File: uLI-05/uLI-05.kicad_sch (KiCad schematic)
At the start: 51 parts, among them J1 STL1550, J2 USB_B, J3 RJ25, J4 RJ25, J5 PROG, Q1 IRF7306, U1 LM78M05_TO252, U2 PC817, U3 PC817, U4 PIC18F14K50-EP, U5 ADM2483xRW, U6 USBLC6-2SC6, Y1 12MHz

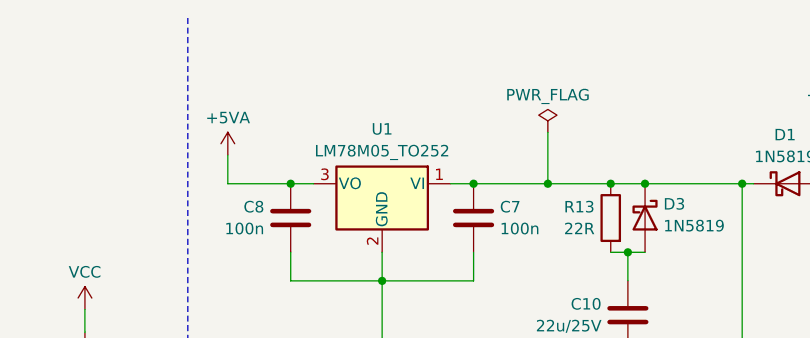
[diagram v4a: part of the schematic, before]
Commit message: pcb: wire XpressNET part.
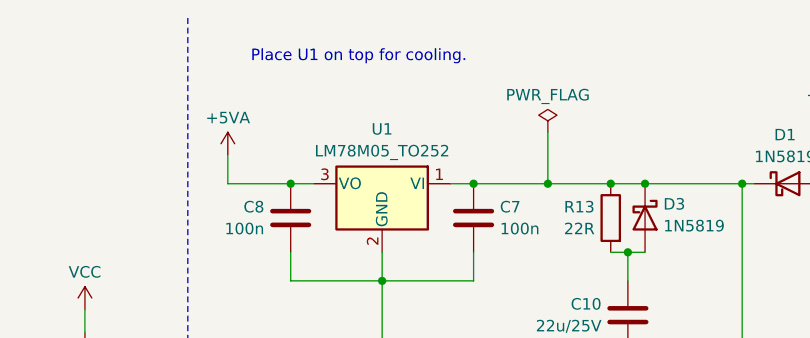
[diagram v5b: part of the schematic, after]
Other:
- note added: "Place U1 on top for cooling."
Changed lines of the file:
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@@
+    (effects (font (size 1.27 1.27)) (justify left bottom))
+  )
+  (text "Place U1 on top for cooling." (at 193.675 19.05 0)
     (effects (font (size 1.27 1.27)) (justify left bottom))
   )

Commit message: Add LCSC numbers.
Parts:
- C1, C2: LCSC (none) -> C1804
- C10: LCSC (none) -> C45783
- C3, C4, C6, C7, C8: LCSC (none) -> C49678
- C5: LCSC (none) -> C13967
- D1, D2: LCSC (none) -> C191023
- D10, D4, D5, D8, D9, H1, H2, J1, J2, J3, J4, J5, JP1, JP2, U1, U2, U3, U6, Y1: JLCPCB_IGNORE (none) -> true
- D3: JLCPCB_CORRECTION (none) -> 0;0;180; LCSC (none) -> C191023
- D7: LCSC (none) -> C32677
- Q1: LCSC (none) -> C879047
- R1, R11, R5, R6, R7, R8: LCSC (none) -> C17520
- R10, R12, R14, R15, R16, R2: LCSC (none) -> C17414
- R13: LCSC (none) -> C17561
- R3, R4: LCSC (none) -> C149504
- R9: LCSC (none) -> C17513
- U4: JLCPCB_CORRECTION (none) -> 0;0;-90; LCSC (none) -> C12460
- U5: JLCPCB_CORRECTION (none) -> 0;0;90; LCSC (none) -> C386280

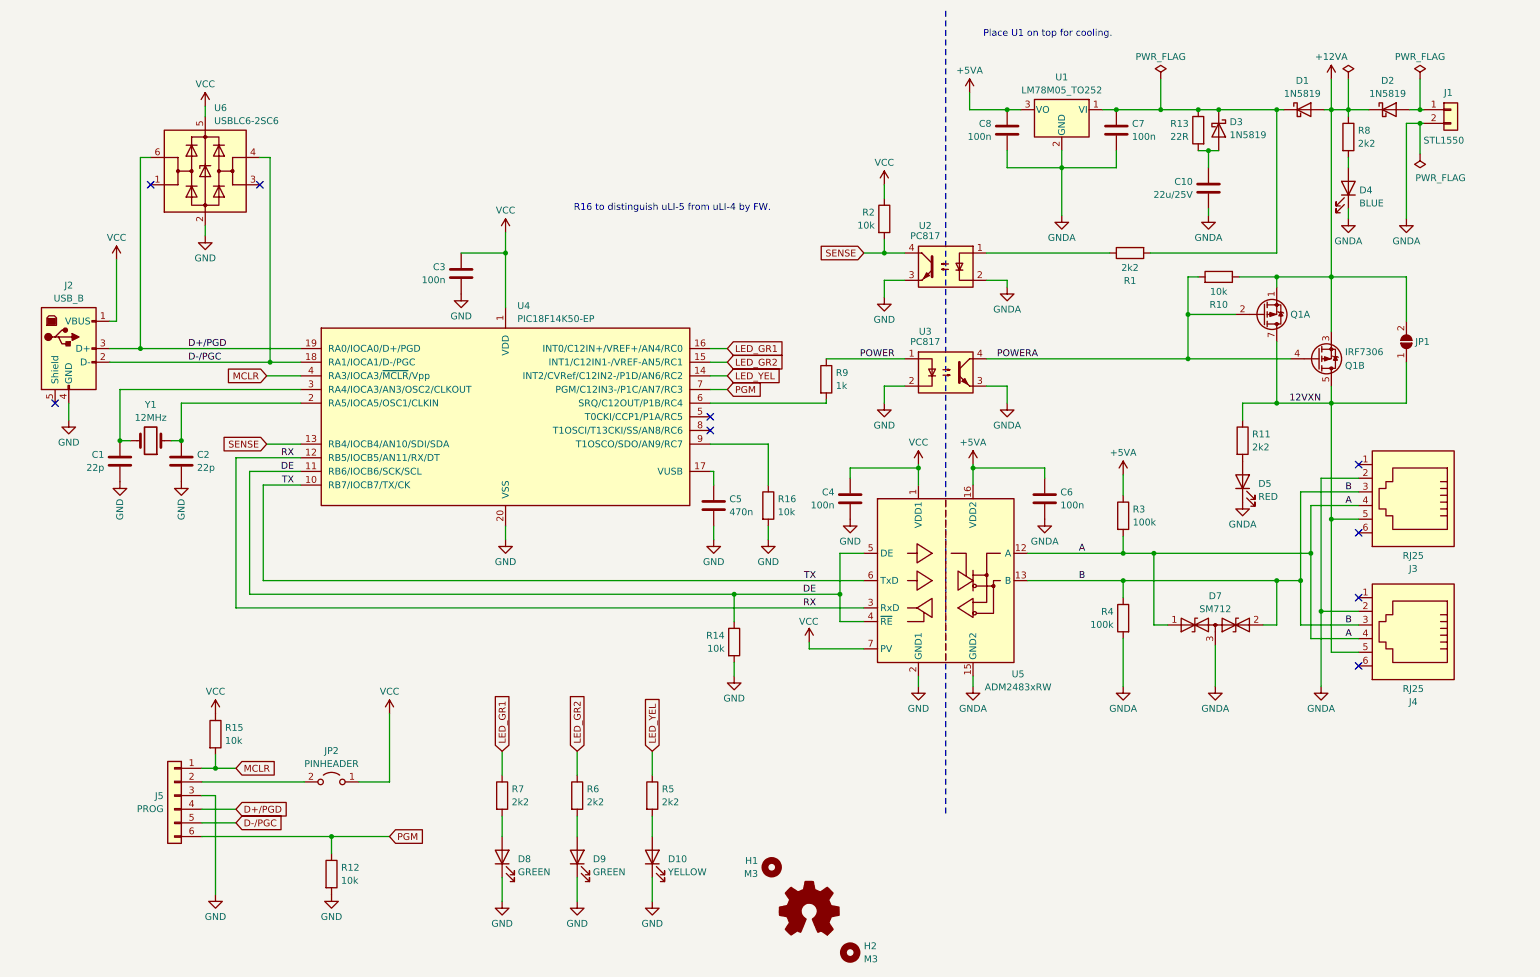
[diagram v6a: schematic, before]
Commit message: Add fuses.
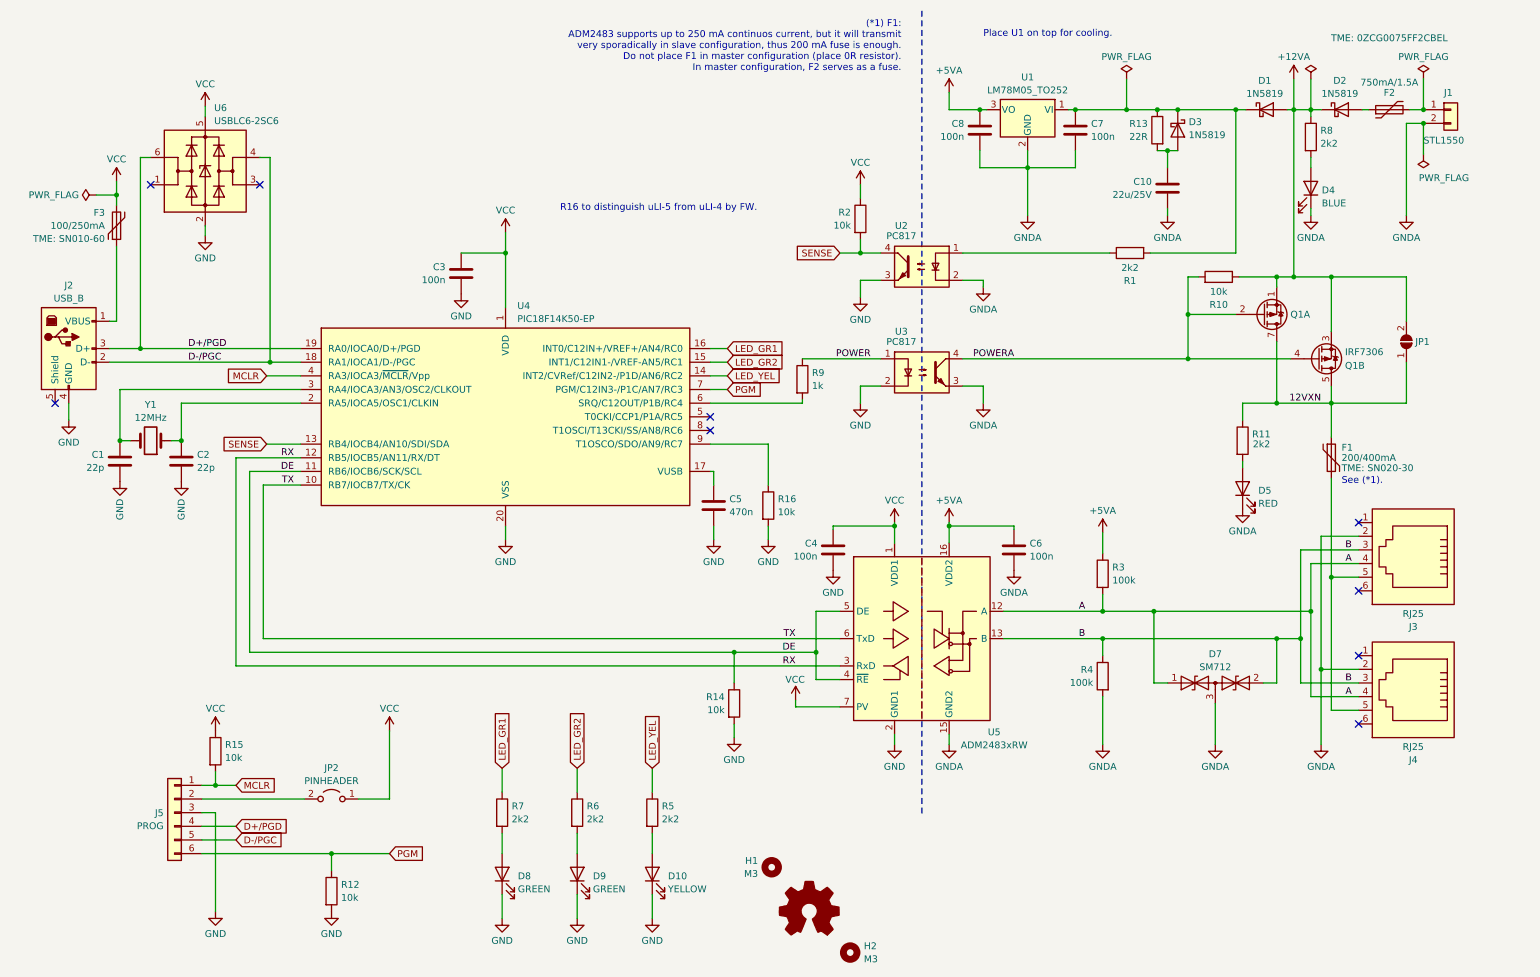
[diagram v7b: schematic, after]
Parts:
- added F1: 200/400mA, Fuse:Fuse_1206_3216Metric, symbol Device:Polyfuse
- added F2: 750mA/1.5A, Fuse:Fuse_1812_4532Metric, symbol Device:Polyfuse
- added F3: 100/250mA, Fuse:Fuse_1206_3216Metric, symbol Device:Polyfuse
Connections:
- net 12VXN: now also F1.1; no longer J3.5, J4.5
- net VCC: now also F3.2; no longer J2.1 (VBUS)
- net at J1.1 (Pin_1): now also F2.2; no longer D2.2 (A)
- new net: F1.2, J3.5, J4.5
- new net: F3.1, J2.1 (VBUS)
- new net: D2.2 (A), F2.1
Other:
- note added: "(*1) F1: ADM2483 supports up to 250 mA continuos current, but it will transmit very sporadically in slave configuration, thus 200 mA fuse is enough. Do not place F1 in master configuration (place 0R resistor). In master configuration, F2 serves as a fuse."
- note added: "See (*1)."
- moved on the sheet: C10, C4, C6, C7, C8, D1, D10, D2, D3, D4, D5, D7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

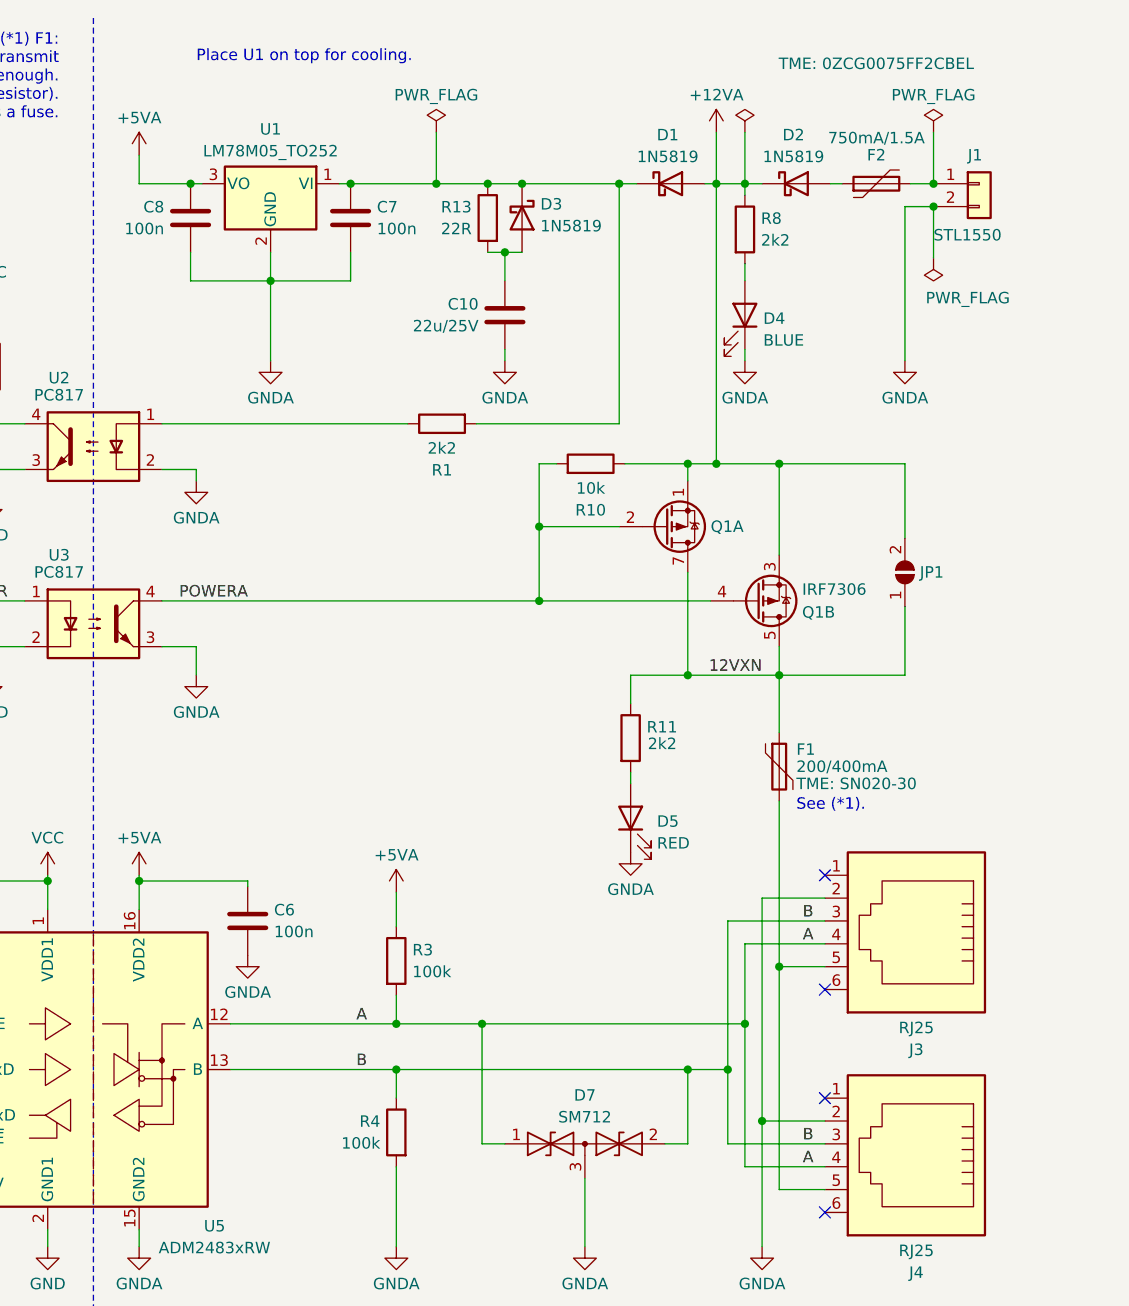
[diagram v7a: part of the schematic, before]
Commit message: Use SS34 as D2.
SS34 supports larger maximum current.
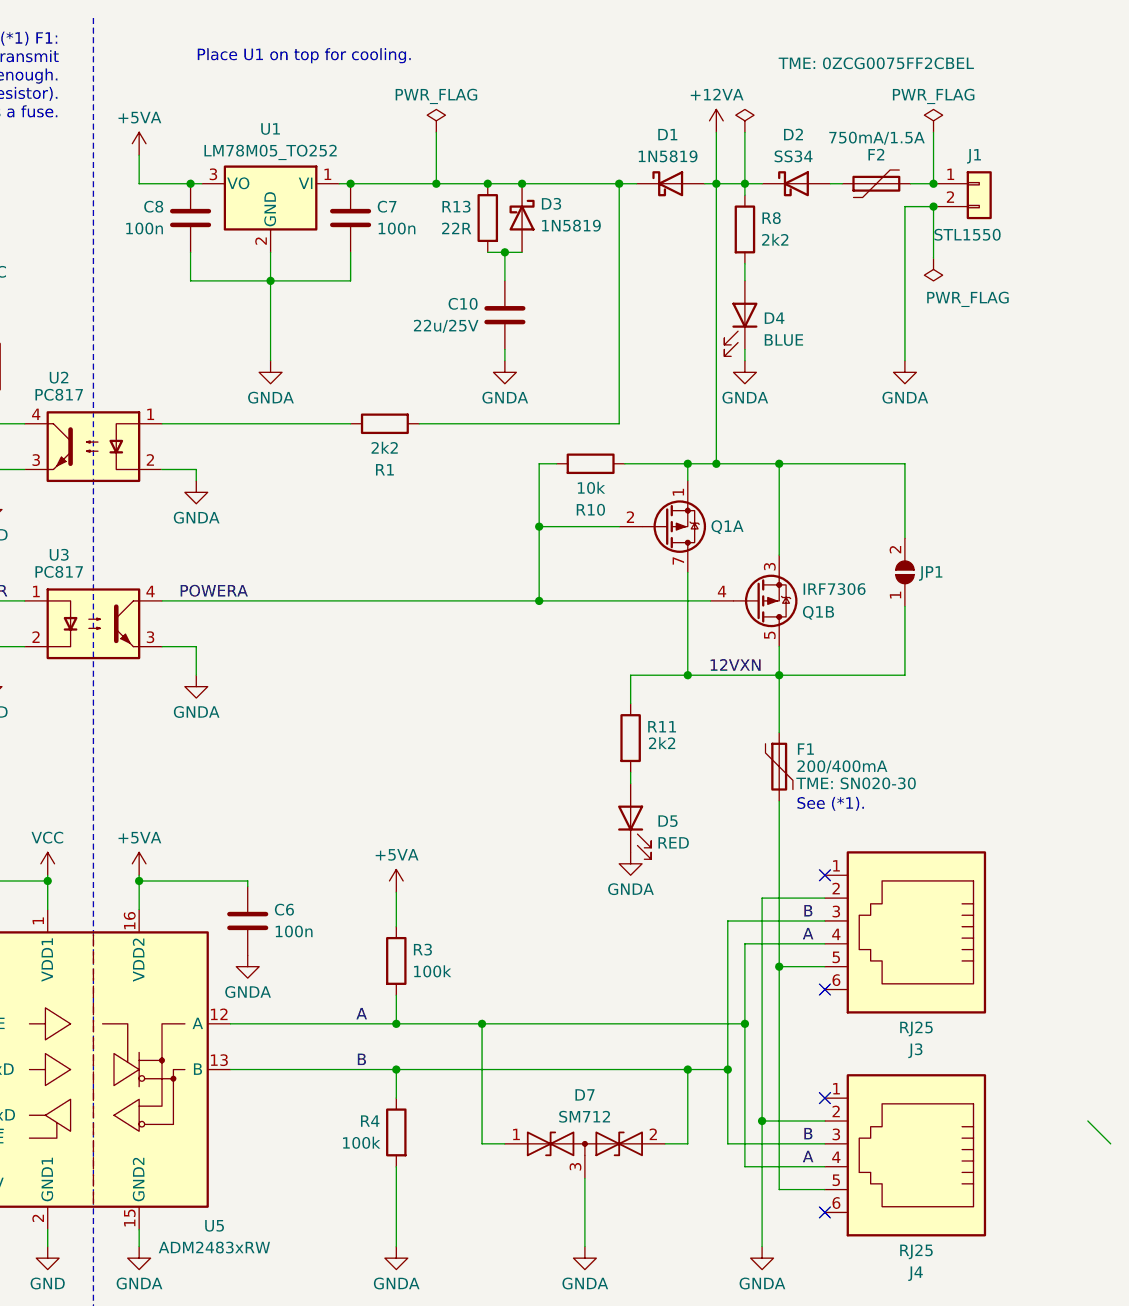
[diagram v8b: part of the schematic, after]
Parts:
- D2: value 1N5819 -> SS34; footprint Diode_SMD:D_SOD-123 -> Diode_SMD:D_SMA; LCSC C191023 -> C8678
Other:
- moved on the sheet: R1
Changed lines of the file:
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@@
   (no_connect (at 38.735 46.355))
   (no_connect (at 263.525 146.685))
+  (bus_entry (at 292.735 136.525) (size 2.54 2.54)
+    (stroke (width 0) (type default))
+  )
   (wire (pts (xy 227.965 40.005) (xy 229.87 40.005))
     (stroke (width 0) (type default))
@@
     (stroke (width 0) (type default))
   )
-  (wire (pts (xy 224.79 59.055) (xy 240.665 59.055))
+  (wire (pts (xy 218.44 59.055) (xy 240.665 59.055))
     (stroke (width 0) (type default))
   )
@@
     (stroke (width 0) (type default))
   )
-  (wire (pts (xy 189.865 59.055) (xy 217.17 59.055))
+  (wire (pts (xy 189.865 59.055) (xy 210.82 59.055))
     (stroke (width 0) (type default))
   )
@@
       (effects (font (size 1.27 1.27)))
     )
-    (property "Value" "1N5819" (at 260.0325 29.3949 0)
-      (effects (font (size 1.27 1.27)))
-    )
-    (property "Footprint" "Diode_SMD:D_SOD-123" (at 260.35 32.385 0)
+    (property "Value" "SS34" (at 260.0325 29.3949 0)
+      (effects (font (size 1.27 1.27)))
+    )
+    (property "Footprint" "Diode_SMD:D_SMA" (at 260.35 32.385 0)
       (effects (font (size 1.27 1.27)) hide)
     )
@@
       (effects (font (size 1.27 1.27)) hide)
     )
-    (property "LCSC" "C191023" (at 260.35 32.385 0)
+    (property "LCSC" "C8678" (at 260.35 32.385 0)
       (effects (font (size 1.27 1.27)) hide)
     )
@@
     )
   )
-  (symbol (lib_id "Device:R") (at 220.98 59.055 90) (mirror x) (unit 1)
+  (symbol (lib_id "Device:R") (at 214.63 59.055 90) (mirror x) (unit 1)
     (in_bom yes) (on_board yes) (dnp no)
-    (property "Reference" "R1" (at 220.98 64.2153 90)
-      (effects (font (size 1.27 1.27)))
-    )
-    (property "Value" "2k2" (at 220.98 61.7911 90)
-      (effects (font (size 1.27 1.27)))
-    )
-    (property "Footprint" "Resistor_SMD:R_0805_2012Metric" (at 220.98 57.277 90)
-      (effects (font (size 1.27 1.27)) hide)
-    )
-    (property "Datasheet" "~" (at 220.98 59.055 0)
-      (effects (font (size 1.27 1.27)) hide)
-    )
-    (property "LCSC" "C17520" (at 220.98 59.055 0)
-      (effects (font (size 1.27 1.27)) hide)
-    )
+    (property "Reference" "R1" (at 214.63 64.2153 90)
+      (effects (font (size 1.27 1.27)))
+    )
+    (property "Value" "2k2" (at 214.63 61.7911 90)
+      (effects (font (size 1.27 1.27)))
+    )
+    (property "Footprint" "Resistor_SMD:R_0805_2012Metric" (at 214.63 57.277 90)
+      (effects (font (size 1.27 1.27)) hide)
+    )
+    (property "Datasheet" "~" (at 214.63 59.055 0)
+      (effects (font (size 1.27 1.27)) hide)
+    )
+    (property "LCSC" "C17520" (at 214.63 59.055 0)
+      (effects (font (size 1.27 1.27)) hide)
+    )
